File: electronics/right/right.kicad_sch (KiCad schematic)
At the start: 21 parts, among them J1 other_side, J2 mic FF, J3 mic FB, J4 speaker, J5 programming, J6 Batt, SW1 jog stick, SW2 Volume up, SW3 Volume down, U1 ATtiny441-M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

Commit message: schematic done, blocks located, uC1 + PWR routed
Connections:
- net FF_mic_R_+: now reaches J1.10 (Pin_10), J2.1 (Pin_1)
- net HP_R_-: now reaches J1.5 (Pin_5), J4.2 (Pin_2)
- net HP_R_+: now reaches J1.6 (Pin_6), J4.1 (Pin_1)
- net FB_mic_R_-: now reaches J1.7 (Pin_7), J3.2 (Pin_2)
- net FB_mic_R_+: now reaches J1.8 (Pin_8), J3.1 (Pin_1)
- net FF_mic_R_-: now reaches J1.9 (Pin_9), J2.2 (Pin_2)
- no-connect marks 0 -> 2
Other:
- note added: "Ear Sensor R"
- note removed: "Ear Sensor"
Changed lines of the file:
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@@
   (junction (at 116.84 161.29) (diameter 0) (color 0 0 0 0)
   )
+  (no_connect (at 91.44 86.36))
+  (no_connect (at 111.76 158.75))
   (wire (pts (xy 91.44 58.42) (xy 102.87 58.42))
     (stroke (width 0) (type default))
@@
     (stroke (width 0) (type default))
   )
+  (wire (pts (xy 219.71 63.5) (xy 238.76 63.5))
+    (stroke (width 0) (type default))
+  )
   (wire (pts (xy 190.5 134.62) (xy 198.12 134.62))
     (stroke (width 0) (type default))
@@
     (stroke (width 0) (type default))
   )
+  (wire (pts (xy 217.17 66.04) (xy 238.76 66.04))
+    (stroke (width 0) (type default))
+  )
   (polyline (pts (xy 165.1 111.76) (xy 165.1 198.12))
     (stroke (width 0) (type default))
@@
     (stroke (width 0) (type default))
   )
-  (wire (pts (xy 238.76 63.5) (xy 219.71 63.5))
-    (stroke (width 0) (type default))
-  )
   (wire (pts (xy 116.84 133.35) (xy 116.84 138.43))
     (stroke (width 0) (type default))
   )
-  (wire (pts (xy 238.76 71.12) (xy 212.09 71.12))
-    (stroke (width 0) (type default))
-  )
   (wire (pts (xy 124.46 175.26) (xy 124.46 176.53))
     (stroke (width 0) (type default))
@@
     (stroke (width 0) (type default))
   )
+  (wire (pts (xy 212.09 71.12) (xy 238.76 71.12))
+    (stroke (width 0) (type default))
+  )
   (wire (pts (xy 248.92 147.32) (xy 248.92 144.78))
     (stroke (width 0) (type default))
@@
     (stroke (width 0) (type default))
   )
+  (wire (pts (xy 222.25 60.96) (xy 238.76 60.96))
+    (stroke (width 0) (type default))
+  )
   (wire (pts (xy 76.2 96.52) (xy 76.2 99.06))
     (stroke (width 0) (type default))
@@
     (stroke (width 0) (type default))
   )
+  (wire (pts (xy 224.79 58.42) (xy 238.76 58.42))
+    (stroke (width 0) (type default))
+  )
   (wire (pts (xy 204.47 60.96) (xy 214.63 60.96))
     (stroke (width 0) (type default))
@@
     (stroke (width 0) (type default))
   )
-  (wire (pts (xy 224.79 58.42) (xy 238.76 58.42))
-    (stroke (width 0) (type default))
-  )
   (wire (pts (xy 104.14 86.36) (xy 110.49 86.36))
     (stroke (width 0) (type default))
   )
-  (wire (pts (xy 238.76 66.04) (xy 217.17 66.04))
-    (stroke (width 0) (type default))
-  )
   (wire (pts (xy 222.25 40.64) (xy 204.47 40.64))
     (stroke (width 0) (type default))
@@
   )
   (wire (pts (xy 224.79 38.1) (xy 224.79 58.42))
-    (stroke (width 0) (type default))
-  )
-  (wire (pts (xy 238.76 60.96) (xy 222.25 60.96))
     (stroke (width 0) (type default))
   )
@@
     (effects (font (size 5 5)) (justify left bottom))
   )
-  (text "Ear Sensor\n" (at 82.55 120.65 0)
+  (text "Ear Sensor R\n" (at 82.55 120.65 0)
     (effects (font (size 5 5)) (justify left bottom))
   )
@@
     (effects (font (size 5 5)) (justify left bottom))
   )
+  (label "FB_mic_R_-" (at 226.06 66.04 0) (fields_autoplaced)
+    (effects (font (size 1.27 1.27)) (justify left bottom))
+  )
+  (label "HP_R_-" (at 226.06 71.12 0) (fields_autoplaced)
+    (effects (font (size 1.27 1.27)) (justify left bottom))
+  )
+  (label "HP_R_+" (at 226.06 68.58 0) (fields_autoplaced)
+    (effects (font (size 1.27 1.27)) (justify left bottom))
+  )
   (label "~{reset}" (at 191.77 144.78 0) (fields_autoplaced)
     (effects (font (size 1.27 1.27)) (justify left bottom))
@@
   )
   (label "SCK" (at 191.77 139.7 0) (fields_autoplaced)
+    (effects (font (size 1.27 1.27)) (justify left bottom))
+  )
+  (label "FF_mic_R_-" (at 226.06 60.96 0) (fields_autoplaced)
     (effects (font (size 1.27 1.27)) (justify left bottom))
   )
@@
     (effects (font (size 1.27 1.27)) (justify left bottom))
   )
+  (label "FB_mic_R_+" (at 226.06 63.5 0) (fields_autoplaced)
+    (effects (font (size 1.27 1.27)) (justify left bottom))
+  )
+  (label "FF_mic_R_+" (at 226.06 58.42 0) (fields_autoplaced)
+    (effects (font (size 1.27 1.27)) (justify left bottom))
+  )

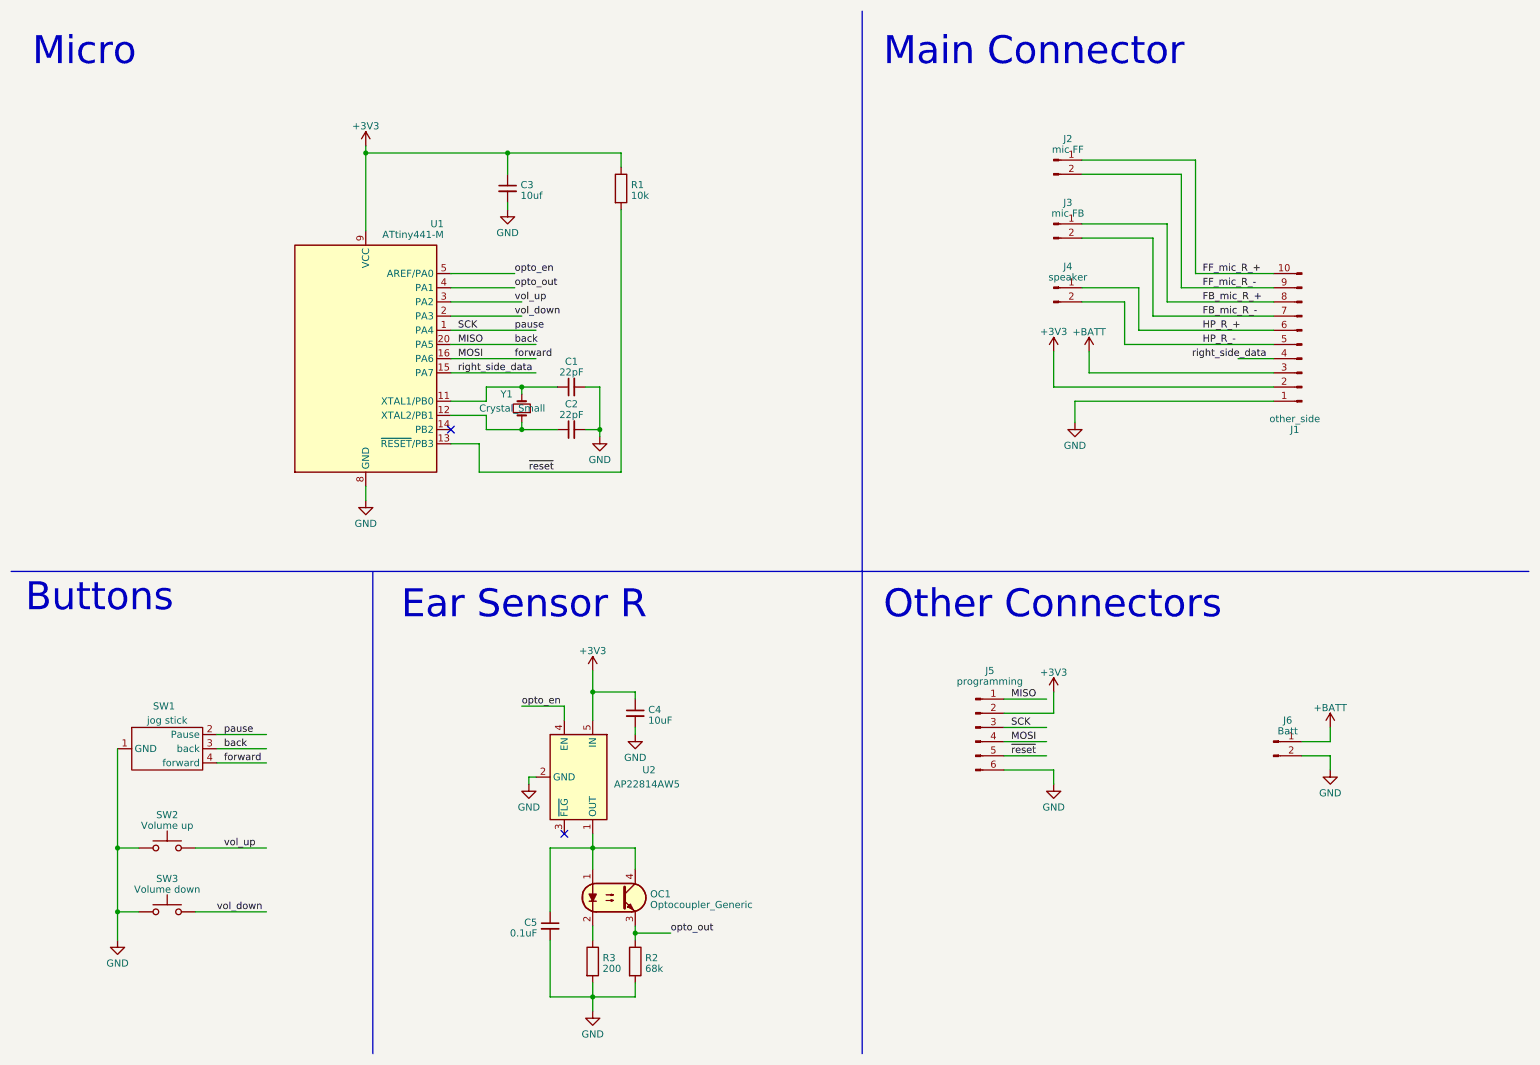
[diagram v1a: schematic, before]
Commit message: pcbs done, filters need to be finalised
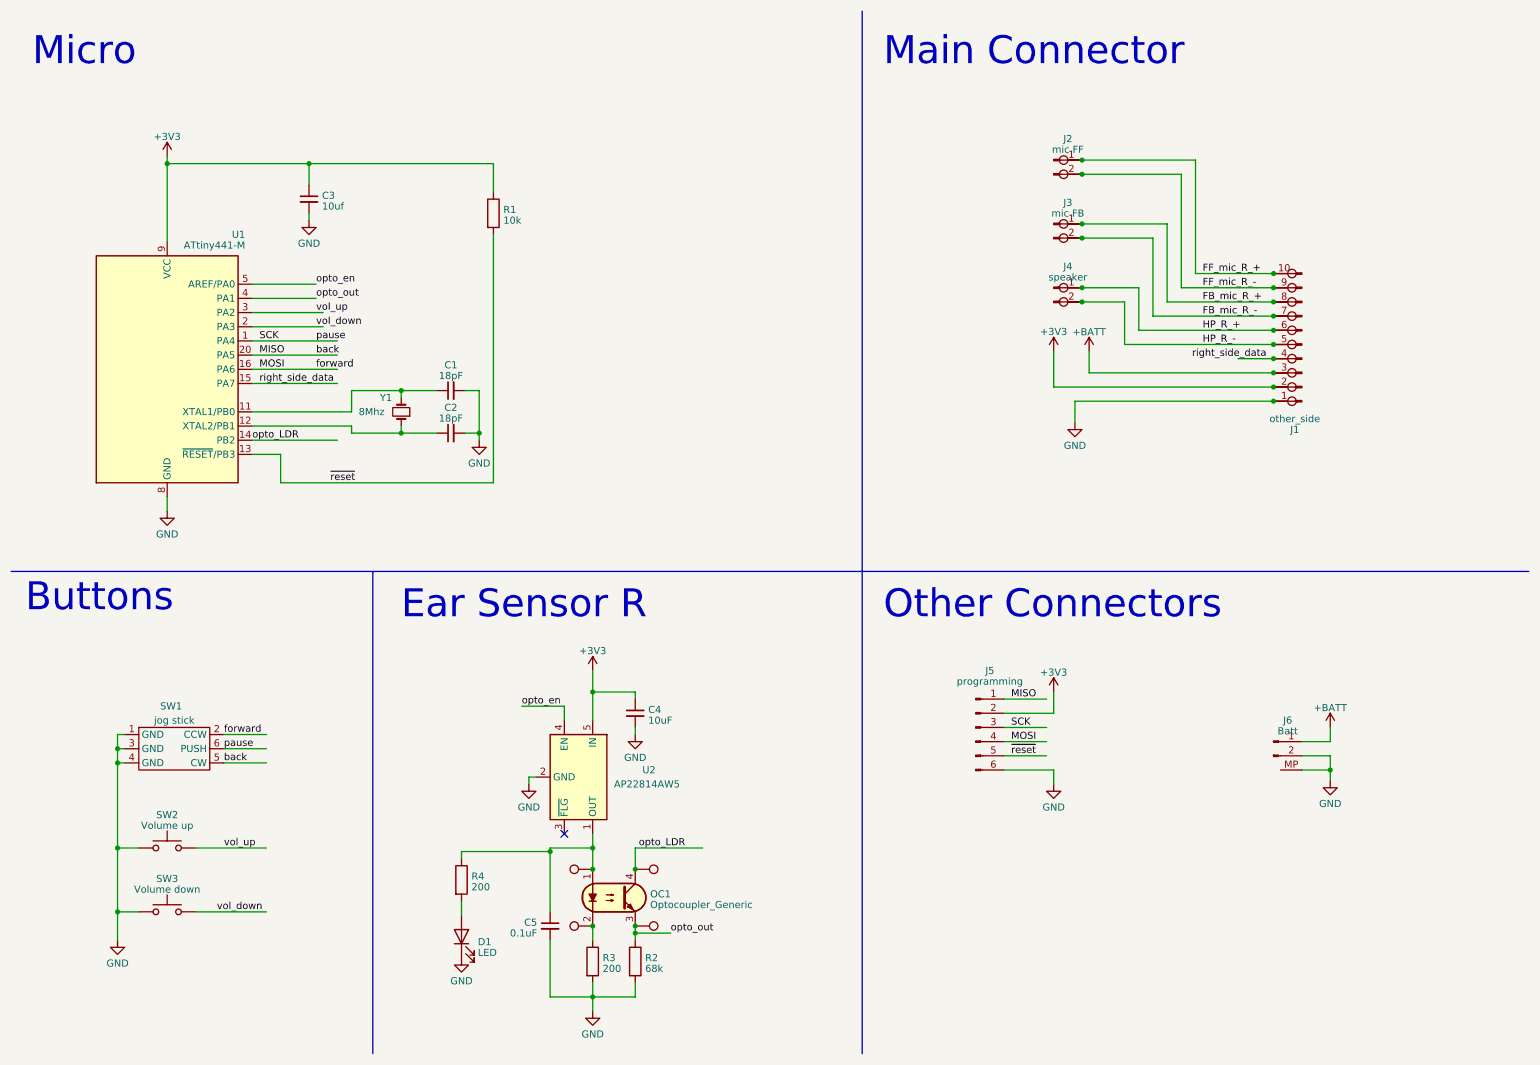
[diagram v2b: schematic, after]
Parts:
- added D1: LED, LED_SMD:LED_0603_1608Metric_Pad1.05x0.95mm_HandSolder, symbol Device:LED
- added R4: 200, Resistor_SMD:R_0402_1005Metric_Pad0.72x0.64mm_HandSolder, symbol Device:R
- added TP1, TP10, TP11, TP12, TP13, TP14, TP15, TP16, TP17, TP18, TP19, TP2, TP20, TP3, TP4, TP5, TP6, TP7, TP8, TP9: TestPoint, TestPoint:TestPoint_Pad_D1.0mm, symbol Connector:TestPoint
- C1, C2: value 22pF -> 18pF; footprint (none) -> Capacitor_SMD:C_0402_1005Metric_Pad0.74x0.62mm_HandSolder
- C3, C4, C5: footprint (none) -> Capacitor_SMD:C_0402_1005Metric_Pad0.74x0.62mm_HandSolder
- J1, J2, J3, J4, OC1: footprint (none) -> X; now left out of the parts list
- J5: footprint (none) -> WE 6 Position SKEDD:490107670612
- J6: footprint (none) -> Connector_JST:JST_SH_BM02B-SRSS-TB_1x02-1MP_P1.00mm_Vertical
- R1, R2, R3: footprint (none) -> Resistor_SMD:R_0402_1005Metric_Pad0.72x0.64mm_HandSolder
- SW1: footprint (none) -> JLS1300-08:JLS1300-08-1F
- SW2, SW3: footprint (none) -> ul_EVQ-P7A01P:EVQ_P7_PAN
- Y1: value Crystal_Small -> 8Mhz; footprint (none) -> Crystal:Crystal_SMD_5032-2Pin_5.0x3.2mm
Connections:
- net +3V3: now also TP8.1
- net +BATT: now also TP9.1
- net FB_mic_R_+: now also TP14.1, TP3.1
- net FB_mic_R_-: now also TP15.1, TP4.1
- net FF_mic_R_+: now also TP1.1, TP16.1
- net FF_mic_R_-: now also TP13.1, TP2.1
- net GND: now also J6.MP, SW1.3 (GND), SW1.4 (GND), D1.1 (K), TP7.1
- net HP_R_+: now also TP10.1, TP5.1
- net HP_R_-: now also TP11.1, TP6.1
- net MISO: now also SW1.5 (CW); no longer SW1.3 (back)
- net MOSI: now also SW1.2 (CCW); no longer SW1.4 (forward)
- net SCK: now also SW1.6 (PUSH); no longer SW1.2 (Pause)
- net opto_out: now also TP19.1
- net right_side_data: now also TP12.1
- net at C5.1, OC1.1, U2.1 (OUT): now also R4.1, TP17.1; no longer OC1.4
- net at OC1.2, R3.1: now also TP18.1
- net opto_LDR: now reaches U1.14 (PB2)
- net opto_LDR: now also OC1.4, TP20.1
- new net: D1.2 (A), R4.2
- no-connect marks 2 -> 1
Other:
- moved on the sheet: C1, C2, C3, R1, U1, Y1
